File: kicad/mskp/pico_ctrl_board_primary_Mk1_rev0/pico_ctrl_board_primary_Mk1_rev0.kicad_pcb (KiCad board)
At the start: 2 copper layers, 47.1 x 62.1 mm, 15 parts, among them J4 USB_C_Receptacle_USB2.0, J7 OLED_128x64, J8 Conn_01x12_Socket, J9 Conn_01x03_Socket, SW3 SW_Omron_B3FS, U1 Raspberry_Pi_Pico

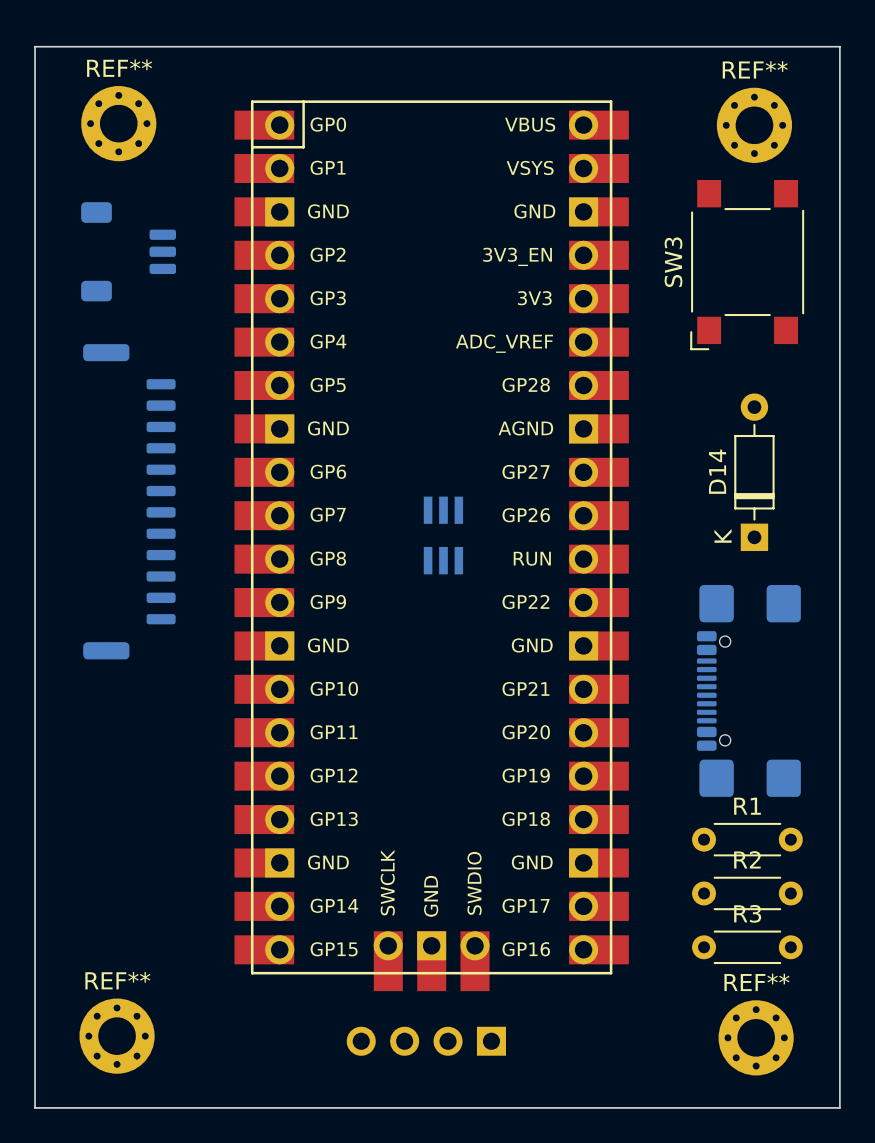
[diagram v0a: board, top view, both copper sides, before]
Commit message: More work on pico layout and start of io shema layout
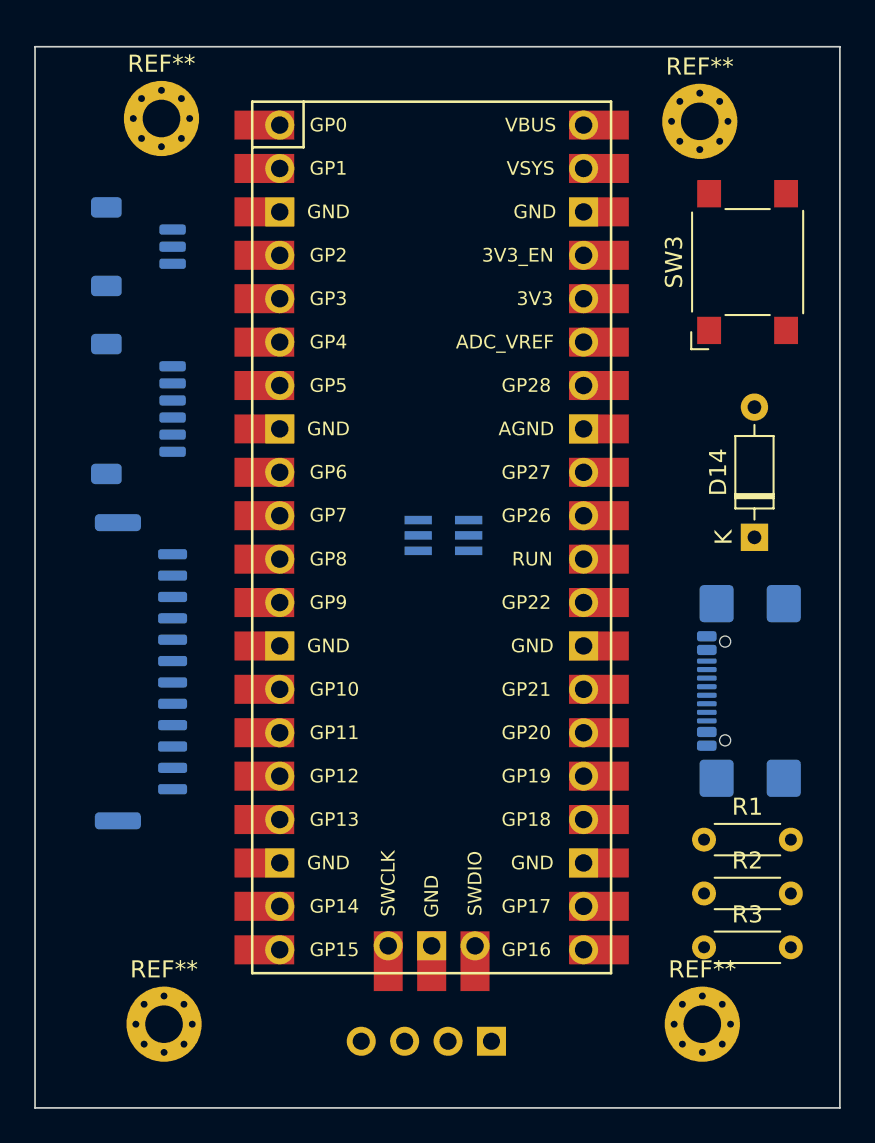
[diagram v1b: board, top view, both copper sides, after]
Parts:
- added J1: Conn_01x06_Socket, Connector_JST:JST_SH_SM06B-SRSS-TB_1x06-1MP_P1.00mm_Horizontal, B.Cu at (130.5, 88.5)
- moved J8 9.97 mm to (130.7, 103.9)
- moved REF** 3.25 mm to (163.5, 124.5)
- moved REF** 3.21 mm to (163.3, 71.7)
- moved REF** 2.84 mm to (132.0, 124.5)
- moved REF** 2.52 mm to (131.8, 71.5)
- moved J9 0.65 mm to (130.5, 79.0)
- turned D1 to 0 degrees
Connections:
- R1 pad 2: Net-(U1-GPIO18) -> Net-(U1-GPIO28_ADC2)
- R2 pad 2: Net-(U1-GPIO17) -> Net-(U1-GPIO27_ADC1)
- R3 pad 2: Net-(U1-GPIO16) -> Net-(U1-GPIO26_ADC0)
- U1 pad 1: Net-(J9-Pin_1) -> Net-(J9-Pin_3)
- U1 pad 10: Net-(J8-Pin_6) -> Net-(J8-Pin_11)
- U1 pad 11: Net-(J8-Pin_7) -> Net-(J8-Pin_10)
- U1 pad 12: Net-(J8-Pin_8) -> Net-(J8-Pin_9)
- U1 pad 14: Net-(J8-Pin_9) -> Net-(J8-Pin_8)
- U1 pad 15: Net-(J8-Pin_10) -> Net-(J8-Pin_7)
- U1 pad 16: Net-(J8-Pin_11) -> Net-(J8-Pin_6)
- U1 pad 17: Net-(J8-Pin_12) -> Net-(J8-Pin_5)
- U1 pad 19: unconnected-(U1-GPIO14-Pad19) -> Net-(J8-Pin_4)
- U1 pad 20: unconnected-(U1-GPIO15-Pad20) -> Net-(J8-Pin_3)
- U1 pad 21: Net-(U1-GPIO16) -> Net-(J8-Pin_2)
- U1 pad 22: Net-(U1-GPIO17) -> Net-(J8-Pin_1)
- U1 pad 24: Net-(U1-GPIO18) -> unconnected-(U1-GPIO18-Pad24)
- U1 pad 3: Net-(J9-Pin_3) -> Net-(J9-Pin_1)
- U1 pad 31: unconnected-(U1-GPIO26_ADC0-Pad31) -> Net-(U1-GPIO26_ADC0)
- U1 pad 32: unconnected-(U1-GPIO27_ADC1-Pad32) -> Net-(U1-GPIO27_ADC1)
- U1 pad 34: unconnected-(U1-GPIO28_ADC2-Pad34) -> Net-(U1-GPIO28_ADC2)
- U1 pad 36: unconnected-(U1-3V3-Pad36) -> Net-(J1-Pin_2)
- U1 pad 4: Net-(J8-Pin_1) -> Net-(J1-Pin_6)
- U1 pad 5: Net-(J8-Pin_2) -> Net-(J1-Pin_5)
- U1 pad 6: Net-(J8-Pin_3) -> Net-(J1-Pin_4)
- U1 pad 7: Net-(J8-Pin_4) -> Net-(J1-Pin_3)
- U1 pad 8: unconnected-(U1-GND-Pad8) -> Net-(J1-Pin_1)
- U1 pad 9: Net-(J8-Pin_5) -> Net-(J8-Pin_12)

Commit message: Adds logo and OSH symbol to all mskp silkscreens
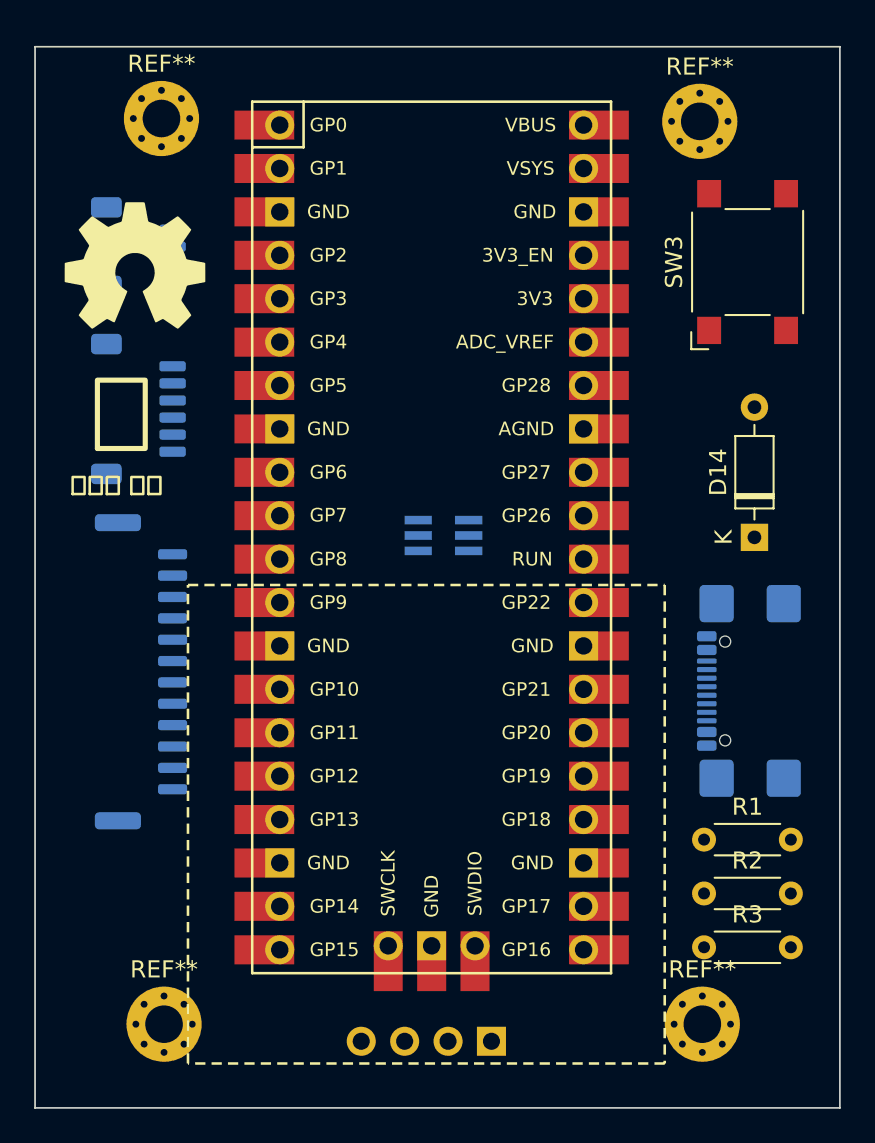
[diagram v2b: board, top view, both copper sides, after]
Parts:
- added G***: LOGO, Desktop:OSH_test, F.Cu at (130.3, 80.1)
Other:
- board text added: "햄"
- board text added: "햄룬드 제조"

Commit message: Adds wiring for pico_ctrl_board_primary_Mk1_rev0
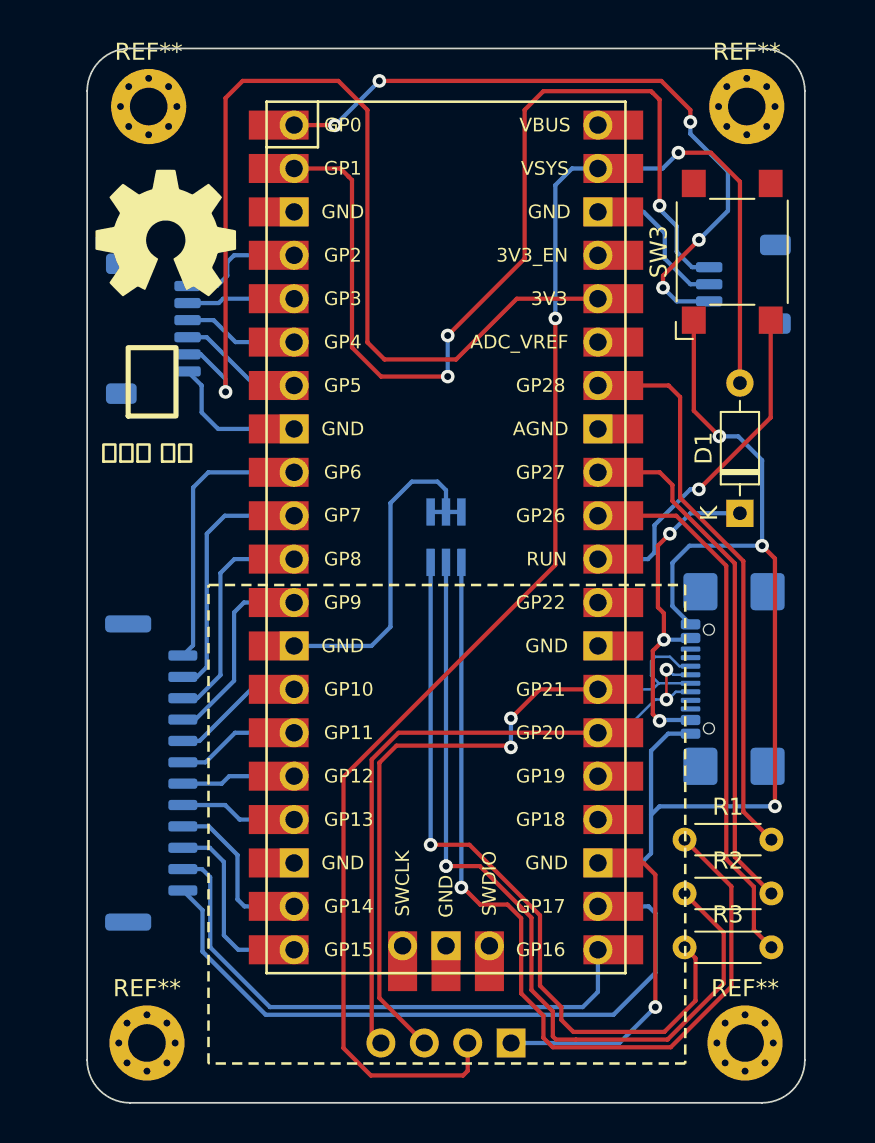
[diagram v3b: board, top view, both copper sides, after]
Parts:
- removed D14: Diode, ScottoKeebs_Components:Diode_DO-35
- added D1: 1N4148, Diode_THT:D_DO-35_SOD27_P7.62mm_Horizontal, F.Cu at (165.7, 94.6)
- moved J4 35.5 mm to (165.9, 81.2), turned to -90 degrees
- moved J2 5.96 mm to (131.2, 109.8)
- moved J3 4.78 mm to (131.4, 83.8)
- moved REF** 2.88 mm to (166.1, 70.8)
- moved REF** 2.73 mm to (166.0, 125.6)
- moved G*** 2.62 mm to (132.1, 78.2)
- moved REF** 1.49 mm to (131.0, 125.6)
- moved J1 1.18 mm to (166.5, 104.3)
- moved U2 1.15 mm to (148.5, 125.6)
- moved R1 1.14 mm to (162.5, 113.7)
- moved R2 1.14 mm to (162.5, 116.8)
- moved R3 1.14 mm to (162.5, 120.0)
- moved SW3 1.08 mm to (165.2, 79.3)
- moved REF** 1.03 mm to (131.1, 70.8)
- moved U1 0.84 mm to (148.5, 96.0)
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- renumbered D1 to D2, J4 to J1, J8 to J2, J1 to J3, J9 to J4, J7 to U2
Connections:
- D2 pad 1: Net-(D1-KB) -> Net-(D2-KB)
- D2 pad 2: Net-(D1-KB) -> Net-(D2-KB)
- D2 pad 3: Net-(D1-KB) -> Net-(D2-KB)
- D2 pad 4: Net-(D1-AR) -> Net-(D2-AR)
- D2 pad 6: Net-(D1-AB) -> Net-(D2-AB)
- J1 pad A1: Net-(J7-GND) -> Net-(U2-GND)
- J1 pad A12: Net-(J7-GND) -> Net-(U2-GND)
- J1 pad B1: Net-(J7-GND) -> Net-(U2-GND)
- J1 pad B12: Net-(J7-GND) -> Net-(U2-GND)
- J4 pad 1: Net-(J9-Pin_1) -> Net-(J4-Pin_1)
- J4 pad 2: Net-(J9-Pin_2) -> GND
- R1 pad 1: Net-(D1-AB) -> Net-(D2-AR)
- R3 pad 1: Net-(D1-AR) -> Net-(D2-AB)
- SW3 pad 1: Net-(SW3-Pad1) -> Net-(U2-GND)
- U1 pad 13: unconnected-(U1-GND-Pad13) -> Net-(D2-KB)
- U1 pad 18: Net-(D1-KB) -> unconnected-(U1-GND-Pad18)
- U1 pad 2: Net-(J9-Pin_2) -> Net-(J4-Pin_1)
- U1 pad 23: Net-(J7-GND) -> Net-(U2-GND)
- U1 pad 28: Net-(SW3-Pad1) -> unconnected-(U1-GND-Pad28)
- U1 pad 3: Net-(J9-Pin_1) -> unconnected-(U1-GND-Pad3)
- U2 pad 1: Net-(J7-GND) -> Net-(U2-GND)
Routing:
- net Net-(D1-A): track 0.00 -> 89.4 mm, vias 0 -> 2
- net Net-(U2-GND): track 0.00 -> 81.0 mm, vias 0 -> 4
- net Net-(J3-Pin_2): track 0.00 -> 59.2 mm, vias 0 -> 1
- net Net-(J4-Pin_1): track 0.00 -> 57.4 mm, vias 0 -> 3
- net Net-(D2-AR): track 0.00 -> 53.2 mm, vias 0 -> 1
- net Net-(D2-AG): track 0.00 -> 49.1 mm, vias 0 -> 1
- net Net-(D2-AB): track 0.00 -> 43.7 mm, vias 0 -> 1
- net Net-(U1-GPIO21): track 0.00 -> 42.8 mm, vias 0 -> 2
- net Net-(J4-Pin_3): track 0.00 -> 40.9 mm, vias 0 -> 5
- net Net-(U1-GPIO20): track 0.00 -> 40.5 mm, vias 0 -> 2
- net Net-(J2-Pin_1): track 0.00 -> 40.1 mm
- net Net-(U1-GPIO28_ADC2): track 0.00 -> 33.2 mm
- net Net-(J2-Pin_2): track 0.00 -> 32.9 mm
- net Net-(U1-GPIO26_ADC0): track 0.00 -> 32.1 mm
- net Net-(U1-GPIO27_ADC1): track 0.00 -> 31.0 mm
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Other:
- board size 47.1 x 62.1 mm -> 42 x 61.7 mm

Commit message: Cleans up unneeded files and adds more silkscreen tidy
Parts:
- moved G*** 1.50 mm to (132.2, 79.7)
- renumbered REF** to H1, REF** to H2, REF** to H3, REF** to H4
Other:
- outline, holes or cut-outs redrawn
- board text added: "03-2024"
- board text added: "GND"
- board text added: "I2C0 BREAKOUT"
- board text added: "JLCJLCJLCJLC"
- board text added: "KEYPAD MODULE"
- board text added: "MSKP-PICO-CTRL-MK.1-REV.0"
- board text added: "Mk 1"
- board text added: "Pico Ctrl Board"
- board text added: "RASPBERRY PI PICO"
- board text added: "RESET"
- board text added: "SCL"
- board text added: "SDA"
- board text added: "SECONDARY CTRL BOARD"
- board text added: "SPI BREAKOUT"
- board text added: "UART DEBUG"
- board text added: "VCC"

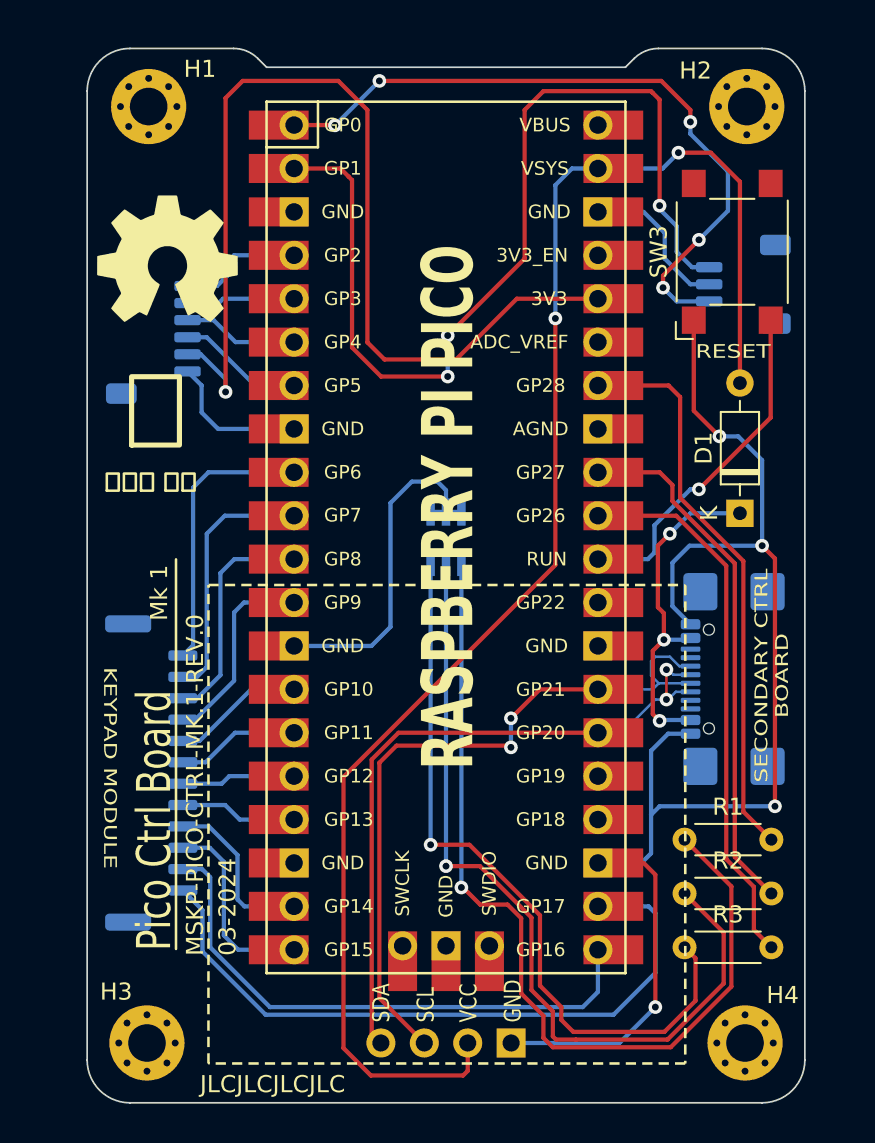
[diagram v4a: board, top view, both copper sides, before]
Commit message: Finalizes mskp pcbs before first run
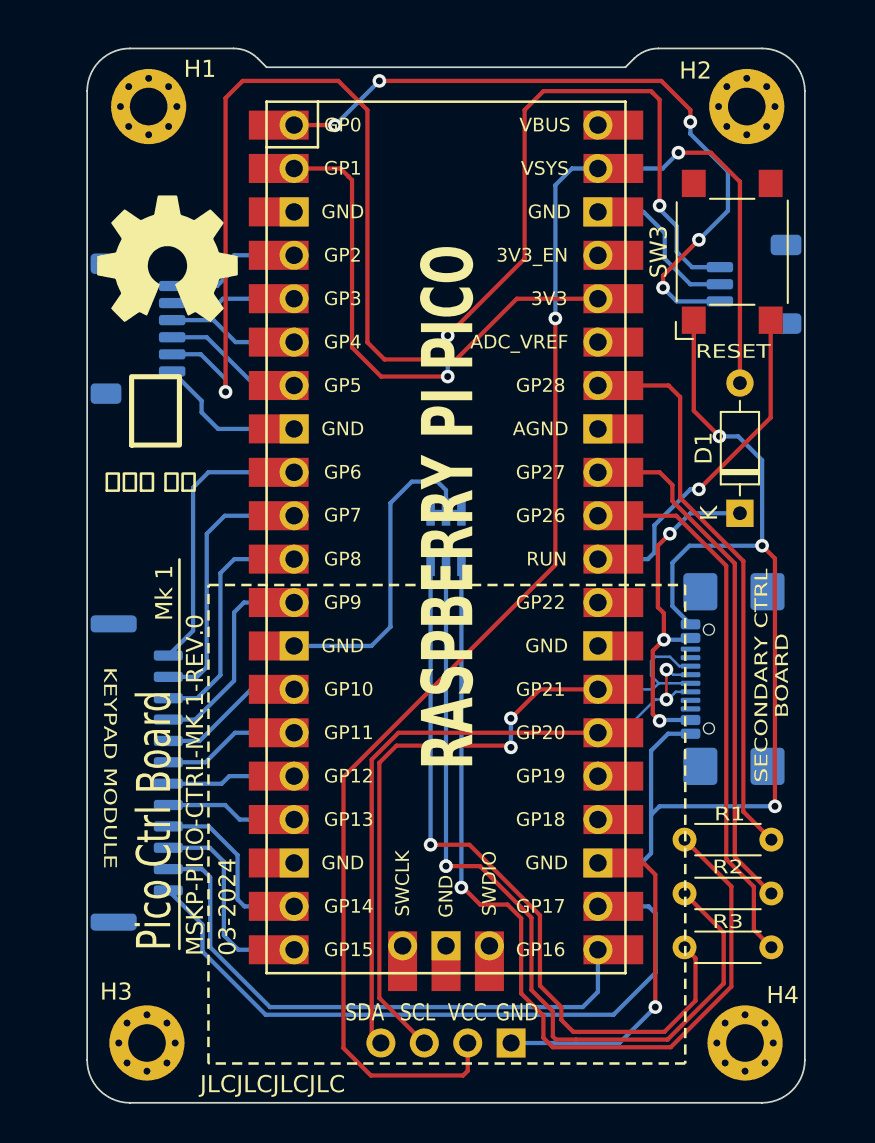
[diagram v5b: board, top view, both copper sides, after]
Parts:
- moved J3 0.90 mm to (130.5, 83.8)
- moved J2 0.85 mm to (130.4, 109.8)
- moved J4 0.62 mm to (166.5, 81.2)
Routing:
- net Net-(J3-Pin_5): track 6.34 -> 7.24 mm
- net Net-(J3-Pin_4): track 6.77 -> 7.67 mm
- net Net-(J3-Pin_3): track 7.41 -> 8.31 mm
- net Net-(J3-Pin_2): track 59.2 -> 60.1 mm
- net Net-(J3-Pin_6): track 7.45 -> 8.35 mm
- net Net-(J2-Pin_6): track 6.69 -> 7.54 mm
- net Net-(J2-Pin_9): track 11.7 -> 12.5 mm
- net Net-(J2-Pin_8): track 7.76 -> 8.61 mm
- net Net-(J2-Pin_7): track 7.23 -> 8.08 mm
- net Net-(J2-Pin_5): track 6.86 -> 7.71 mm
- net Net-(J2-Pin_4): track 9.97 -> 10.8 mm
- net Net-(J2-Pin_3): track 11.5 -> 12.4 mm
- net Net-(J2-Pin_2): track 32.9 -> 33.7 mm
- net Net-(J2-Pin_11): track 15.0 -> 15.8 mm
- net Net-(J2-Pin_10): track 13.4 -> 14.2 mm
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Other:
- board text added: "3V3"
- board text added: "CSn"
- board text added: "RX"
- board text added: "SCK"
- board text added: "TX"
